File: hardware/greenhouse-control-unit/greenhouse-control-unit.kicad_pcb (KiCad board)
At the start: 2 copper layers, 150 x 90 mm, 51 parts, among them J1 Buck_Conn_01x01_Female, J10 Conn_01x08, J11 Conn_01x08, J12 Conn_01x05_Female, J15 Conn_01x05_Female, J16 Conn_01x05_Female, J2 Buck_Conn_01x01_Female, J3 Buck_Conn_01x01_Female, J4 Buck_Conn_01x01_Female, J5 Molex_KK-396_01x02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

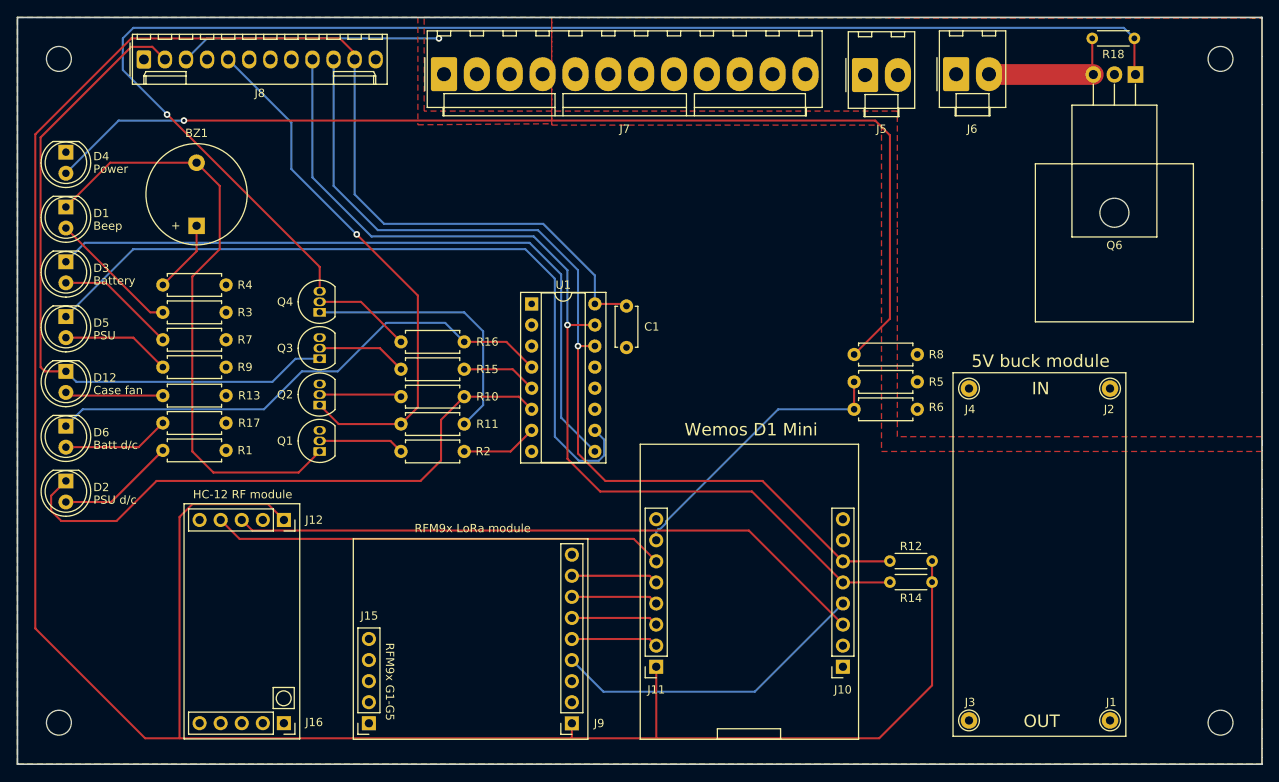
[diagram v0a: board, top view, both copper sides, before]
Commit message: Reposition 10V resistors
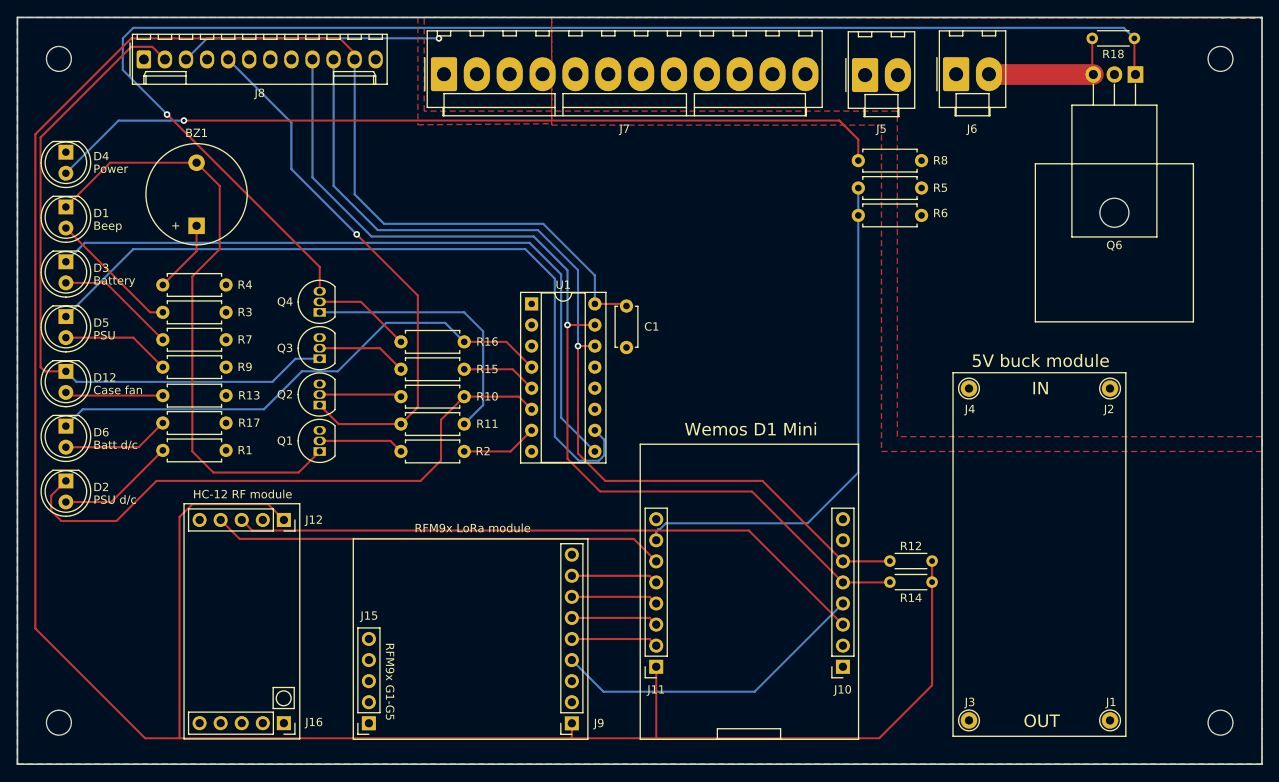
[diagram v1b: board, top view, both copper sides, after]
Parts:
- moved R6 23.4 mm to (173.5, 68.3)
- moved R8 23.4 mm to (181.1, 61.7)
- moved R5 23.4 mm to (181.1, 65.0)
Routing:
- net Net-(D4-Pad2): track 130.9 -> 101.6 mm
- net /A0: track 34.4 -> 62.7 mm
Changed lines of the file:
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@@
   )
   (footprint "Resistor_THT:R_Axial_DIN0207_L6.3mm_D2.5mm_P7.62mm_Horizontal" (layer "F.Cu")
-    (at 180.594 88.392 180)
+    (at 181.102 65.024 180)
     (descr "Resistor, Axial_DIN0207 series, Axial, Horizontal, pin pitch=7.62mm, 0.25W = 1/4W, length*diameter=6.3*2.5mm^2, http://cdn-reichelt.de/documents/datenblatt/B400/1_4W%23YAG.pdf")
     (tags "Resistor Axial_DIN0207 series Axial Horizontal pin pitch 7.62mm 0.25W = 1/4W length 6.3mm diameter 2.5mm")
@@
   )
   (footprint "Resistor_THT:R_Axial_DIN0207_L6.3mm_D2.5mm_P7.62mm_Horizontal" (layer "F.Cu")
-    (at 172.974 91.694)
+    (at 173.482 68.326)
     (descr "Resistor, Axial_DIN0207 series, Axial, Horizontal, pin pitch=7.62mm, 0.25W = 1/4W, length*diameter=6.3*2.5mm^2, http://cdn-reichelt.de/documents/datenblatt/B400/1_4W%23YAG.pdf")
     (tags "Resistor Axial_DIN0207 series Axial Horizontal pin pitch 7.62mm 0.25W = 1/4W length 6.3mm diameter 2.5mm")
@@
   )
   (footprint "Resistor_THT:R_Axial_DIN0207_L6.3mm_D2.5mm_P7.62mm_Horizontal" (layer "F.Cu")
-    (at 180.594 85.09 180)
+    (at 181.102 61.722 180)
     (descr "Resistor, Axial_DIN0207 series, Axial, Horizontal, pin pitch=7.62mm, 0.25W = 1/4W, length*diameter=6.3*2.5mm^2, http://cdn-reichelt.de/documents/datenblatt/B400/1_4W%23YAG.pdf")
     (tags "Resistor Axial_DIN0207 series Axial Horizontal pin pitch 7.62mm 0.25W = 1/4W length 6.3mm diameter 2.5mm")
@@
   (segment (start 114.808 70.866) (end 107.696 63.754) (width 0.25) (layer "B.Cu") (net 24))
   (segment (start 138.43 81.534) (end 138.43 74.93) (width 0.25) (layer "B.Cu") (net 24))
-  (segment (start 172.974 88.392) (end 172.974 91.694) (width 0.25) (layer "F.Cu") (net 26))
-  (segment (start 172.974 91.694) (end 163.83 91.694) (width 0.25) (layer "B.Cu") (net 26))
-  (segment (start 149.126 106.398) (end 149.126 107.4805) (width 0.25) (layer "B.Cu") (net 26))
-  (segment (start 150.300511 105.426999) (end 149.612499 106.115011) (width 0.25) (layer "B.Cu") (net 26))
-  (segment (start 149.408989 106.115011) (end 149.126 106.398) (width 0.25) (layer "B.Cu") (net 26))
-  (segment (start 149.612499 106.115011) (end 149.408989 106.115011) (width 0.25) (layer "B.Cu") (net 26))
-  (segment (start 163.83 91.694) (end 150.300511 105.223489) (width 0.25) (layer "B.Cu") (net 26))
-  (segment (start 150.300511 105.223489) (end 150.300511 105.426999) (width 0.25) (layer "B.Cu") (net 26))
+  (segment (start 149.612499 106.115011) (end 150.300511 105.426999) (width 0.25) (layer "B.Cu") (net 26))
+  (segment (start 173.482 68.326) (end 173.482 99.314) (width 0.25) (layer "B.Cu") (net 26))
+  (segment (start 150.300511 105.426999) (end 167.369001 105.426999) (width 0.25) (layer "B.Cu") (net 26))
+  (segment (start 149.126 106.398) (end 149.408989 106.115011) (width 0.25) (layer "B.Cu") (net 26))
+  (segment (start 149.126 107.4805) (end 149.126 106.398) (width 0.25) (layer "B.Cu") (net 26))
+  (segment (start 173.482 65.024) (end 173.482 68.326) (width 0.25) (layer "B.Cu") (net 26))
+  (segment (start 149.408989 106.115011) (end 149.612499 106.115011) (width 0.25) (layer "B.Cu") (net 26))
+  (segment (start 167.369001 105.426999) (end 173.482 99.314) (width 0.25) (layer "B.Cu") (net 26))
   (segment (start 75.433 87.122) (end 77.978 87.122) (width 0.25) (layer "F.Cu") (net 40))
   (segment (start 85.852 48.006) (end 88.392 48.006) (width 0.25) (layer "F.Cu") (net 40))
@@
   (segment (start 88.138 80.01) (end 89.662 80.01) (width 0.25) (layer "F.Cu") (net 41))
   (segment (start 77.978 69.85) (end 88.138 80.01) (width 0.25) (layer "F.Cu") (net 41))
-  (segment (start 92.202 56.896) (end 175.514 56.896) (width 0.25) (layer "F.Cu") (net 42))
-  (segment (start 177.292 58.674) (end 177.292 80.772) (width 0.25) (layer "F.Cu") (net 42))
-  (segment (start 177.292 80.772) (end 172.974 85.09) (width 0.25) (layer "F.Cu") (net 42))
-  (segment (start 175.514 56.896) (end 177.292 58.674) (width 0.25) (layer "F.Cu") (net 42))
+  (segment (start 171.196 56.896) (end 173.482 59.182) (width 0.25) (layer "F.Cu") (net 42))
+  (segment (start 173.482 59.182) (end 173.482 61.722) (width 0.25) (layer "F.Cu") (net 42))
+  (segment (start 92.202 56.896) (end 171.196 56.896) (width 0.25) (layer "F.Cu") (net 42))
   (via (at 92.202 56.896) (size 0.8) (drill 0.4) (layers "F.Cu" "B.Cu") (net 42))
   (segment (start 84.328 56.896) (end 77.978 63.246) (width 0.25) (layer "B.Cu") (net 42))

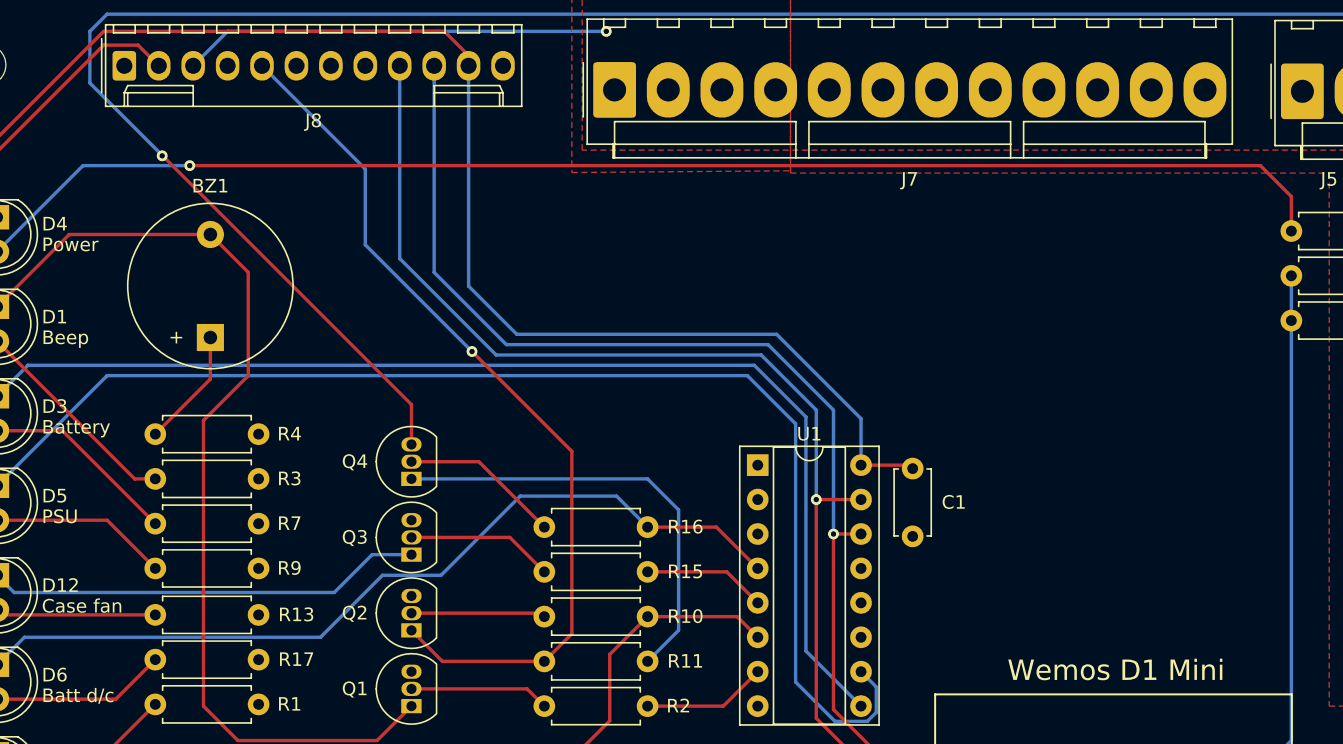
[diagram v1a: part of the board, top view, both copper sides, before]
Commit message: Fixed ground plane island
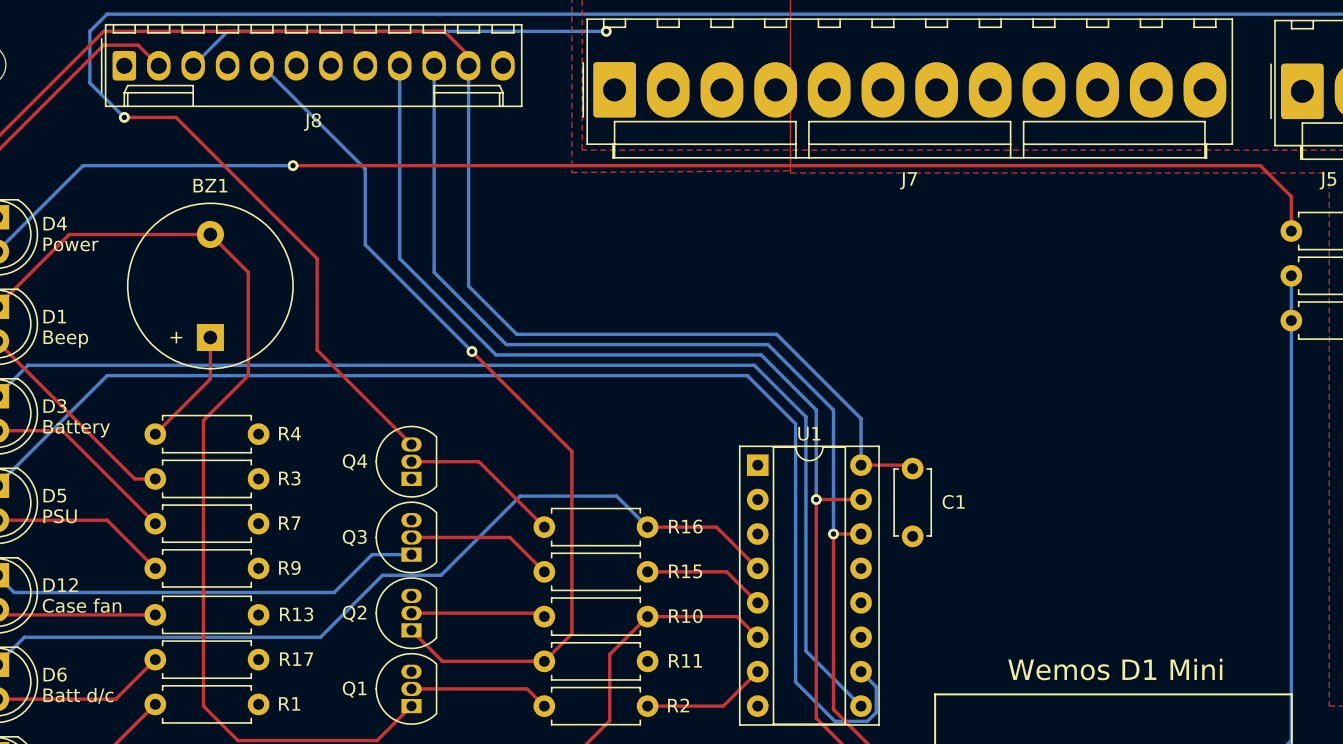
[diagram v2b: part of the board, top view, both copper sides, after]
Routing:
- net +5V: track 32.8 -> 0.00 mm
- net Net-(Q6-Pad1): track 167.7 -> 169.9 mm
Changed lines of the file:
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@@
   (segment (start 93.726 72.644) (end 89.662 76.708) (width 0.25) (layer "F.Cu") (net 2))
   (segment (start 93.726 69.576) (end 93.726 72.644) (width 0.25) (layer "F.Cu") (net 2))
-  (segment (start 128.27 82.296) (end 125.984 80.01) (width 0.25) (layer "B.Cu") (net 3))
-  (segment (start 125.984 93.472) (end 128.27 91.186) (width 0.25) (layer "B.Cu") (net 3))
-  (segment (start 125.984 80.01) (end 108.564 80.01) (width 0.25) (layer "B.Cu") (net 3))
-  (segment (start 128.27 91.186) (end 128.27 82.296) (width 0.25) (layer "B.Cu") (net 3))
   (segment (start 82.804 76.454) (end 77.978 76.454) (width 0.25) (layer "F.Cu") (net 4))
   (segment (start 89.662 83.312) (end 82.804 76.454) (width 0.25) (layer "F.Cu") (net 4))
@@
   (segment (start 142.856511 95.358511) (end 141.732 94.234) (width 0.25) (layer "B.Cu") (net 11))
   (segment (start 77.978 80.518) (end 86.101 72.395) (width 0.25) (layer "B.Cu") (net 11))
-  (segment (start 90.17 56.1715) (end 90.2075 56.1715) (width 0.25) (layer "F.Cu") (net 12))
+  (segment (start 101.6 70.506) (end 108.564 77.47) (width 0.25) (layer "F.Cu") (net 12))
   (segment (start 206.756 46.99) (end 206.756 51.2149) (width 0.25) (layer "F.Cu") (net 12))
   (segment (start 206.756 51.2149) (end 206.8876 51.3465) (width 0.25) (layer "F.Cu") (net 12))
-  (segment (start 108.564 74.528) (end 108.564 77.47) (width 0.25) (layer "F.Cu") (net 12))
-  (segment (start 90.2075 56.1715) (end 108.564 74.528) (width 0.25) (layer "F.Cu") (net 12))
-  (via (at 90.17 56.1715) (size 0.8) (drill 0.4) (layers "F.Cu" "B.Cu") (net 12))
+  (segment (start 91.186 53.34) (end 101.6 63.754) (width 0.25) (layer "F.Cu") (net 12))
+  (segment (start 87.376 53.34) (end 91.186 53.34) (width 0.25) (layer "F.Cu") (net 12))
+  (segment (start 101.6 63.754) (end 101.6 70.506) (width 0.25) (layer "F.Cu") (net 12))
+  (via (at 87.376 53.34) (size 0.8) (drill 0.4) (layers "F.Cu" "B.Cu") (net 12))
+  (segment (start 84.836 50.8) (end 84.836 46.99) (width 0.25) (layer "B.Cu") (net 12))
   (segment (start 205.486 45.72) (end 206.756 46.99) (width 0.25) (layer "B.Cu") (net 12))
-  (segment (start 84.836 50.8) (end 84.836 46.99) (width 0.25) (layer "B.Cu") (net 12))
   (segment (start 84.836 46.99) (end 86.106 45.72) (width 0.25) (layer "B.Cu") (net 12))
-  (segment (start 90.17 56.134) (end 84.836 50.8) (width 0.25) (layer "B.Cu") (net 12))
-  (segment (start 90.17 56.1715) (end 90.17 56.134) (width 0.25) (layer "B.Cu") (net 12))
   (segment (start 86.106 45.72) (end 205.486 45.72) (width 0.25) (layer "B.Cu") (net 12))
+  (segment (start 87.376 53.34) (end 84.836 50.8) (width 0.25) (layer "B.Cu") (net 12))
   (segment (start 125.984 96.774) (end 131.572 96.774) (width 0.25) (layer "F.Cu") (net 13))
   (segment (start 131.572 96.774) (end 134.112 94.234) (width 0.25) (layer "F.Cu") (net 13))
@@
   (segment (start 77.978 69.85) (end 88.138 80.01) (width 0.25) (layer "F.Cu") (net 41))
   (segment (start 171.196 56.896) (end 173.482 59.182) (width 0.25) (layer "F.Cu") (net 42))
+  (segment (start 99.822 56.896) (end 171.196 56.896) (width 0.25) (layer "F.Cu") (net 42))
   (segment (start 173.482 59.182) (end 173.482 61.722) (width 0.25) (layer "F.Cu") (net 42))
-  (segment (start 92.202 56.896) (end 171.196 56.896) (width 0.25) (layer "F.Cu") (net 42))
-  (via (at 92.202 56.896) (size 0.8) (drill 0.4) (layers "F.Cu" "B.Cu") (net 42))
+  (via (at 99.822 56.896) (size 0.8) (drill 0.4) (layers "F.Cu" "B.Cu") (net 42))
   (segment (start 84.328 56.896) (end 77.978 63.246) (width 0.25) (layer "B.Cu") (net 42))
-  (segment (start 92.202 56.896) (end 84.328 56.896) (width 0.25) (layer "B.Cu") (net 42))
+  (segment (start 99.822 56.896) (end 84.328 56.896) (width 0.25) (layer "B.Cu") (net 42))
   (segment (start 89.662 90.043) (end 78.359 90.043) (width 0.25) (layer "F.Cu") (net 43))
   (segment (start 78.359 90.043) (end 77.978 89.662) (width 0.25) (layer "F.Cu") (net 43))

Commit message: Changed track
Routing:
- net Net-(Q1-Pad1): track 72.7 -> 73.3 mm
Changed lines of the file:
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@@
   (segment (start 118.364 96.774) (end 117.094 95.504) (width 0.25) (layer "F.Cu") (net 15))
   (segment (start 117.094 95.504) (end 108.564 95.504) (width 0.25) (layer "F.Cu") (net 15))
-  (segment (start 83.307 61.976) (end 93.726 61.976) (width 0.25) (layer "F.Cu") (net 16))
+  (segment (start 96.52 72.39) (end 96.52 67.31) (width 0.25) (layer "F.Cu") (net 16))
   (segment (start 93.218 96.774) (end 95.758 99.314) (width 0.25) (layer "F.Cu") (net 16))
   (segment (start 95.758 99.314) (end 106.024 99.314) (width 0.25) (layer "F.Cu") (net 16))
+  (segment (start 77.978 67.31) (end 96.52 67.31) (width 0.25) (layer "F.Cu") (net 16))
   (segment (start 93.218 96.774) (end 93.218 75.692) (width 0.25) (layer "F.Cu") (net 16))
   (segment (start 106.024 99.314) (end 108.564 96.774) (width 0.25) (layer "F.Cu") (net 16))
-  (segment (start 83.307 61.981) (end 83.307 61.976) (width 0.25) (layer "F.Cu") (net 16))
   (segment (start 96.52 64.77) (end 93.726 61.976) (width 0.25) (layer "F.Cu") (net 16))
   (segment (start 93.218 75.692) (end 96.52 72.39) (width 0.25) (layer "F.Cu") (net 16))
-  (segment (start 77.978 67.31) (end 83.307 61.981) (width 0.25) (layer "F.Cu") (net 16))
-  (segment (start 96.52 72.39) (end 96.52 64.77) (width 0.25) (layer "F.Cu") (net 16))
+  (segment (start 96.52 67.31) (end 96.52 64.77) (width 0.25) (layer "F.Cu") (net 16))
   (segment (start 115.824 84.328) (end 108.564 84.328) (width 0.25) (layer "F.Cu") (net 17))
   (segment (start 118.364 86.868) (end 115.824 84.328) (width 0.25) (layer "F.Cu") (net 17))
